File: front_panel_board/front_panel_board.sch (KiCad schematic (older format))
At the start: 4 parts

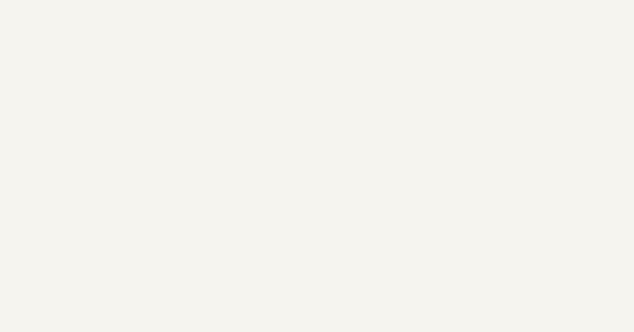
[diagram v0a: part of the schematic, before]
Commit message: update TODO on front panel board (headphone amp)
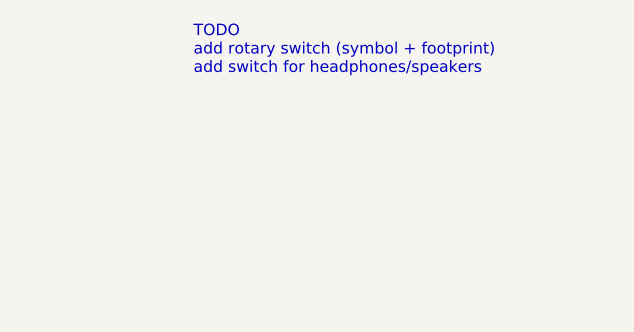
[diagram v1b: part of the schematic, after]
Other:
- note added: "TODO\nadd rotary switch (symbol + footprint)\nadd switch for headphones/speakers"
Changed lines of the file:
@@
 	1    0    0    -1
 $EndComp
+Text Notes 8800 1000 0    50   ~ 0
+TODO\nadd rotary switch (symbol + footprint)\nadd switch for headphones/speakers
 $EndSCHEMATC

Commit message: draw initial schematic for front panel board. Resistor sizing and component selection still todo
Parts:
- removed J?: Conn_02x04_Odd_Even, symbol Connector_Generic:Conn_02x04_Odd_Even
- added J2: Conn_02x05_Odd_Even, symbol Connector_Generic:Conn_02x05_Odd_Even
- added R1, R2: R, symbol Device:R
- added SW1: SW_Rotary4, symbol Switch_gkeeth:SW_Rotary4
- added SW2: SW_SPST, symbol Switch:SW_SPST
- gave numbers to parts that had none: 3
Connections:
- net labels added: GNDRELAY, Vrelay, input1_select, input2_select, input3_select, input4_select, output_mute_select
- wire segments 0 -> 32
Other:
- note added: "TODO\nadd rotary switch footprint\nsize relay resistors"
- note added: "disables main preamp output\n(headphones unaffected)"
- note added: "input selection switch"
- note added: "output mute switch"
- note added: "power LED"
- note added: "power connector"
- note removed: "TODO\nadd rotary switch (symbol + footprint)\nadd switch for headphones/speakers"
- moved on the sheet: D1, J1, R3

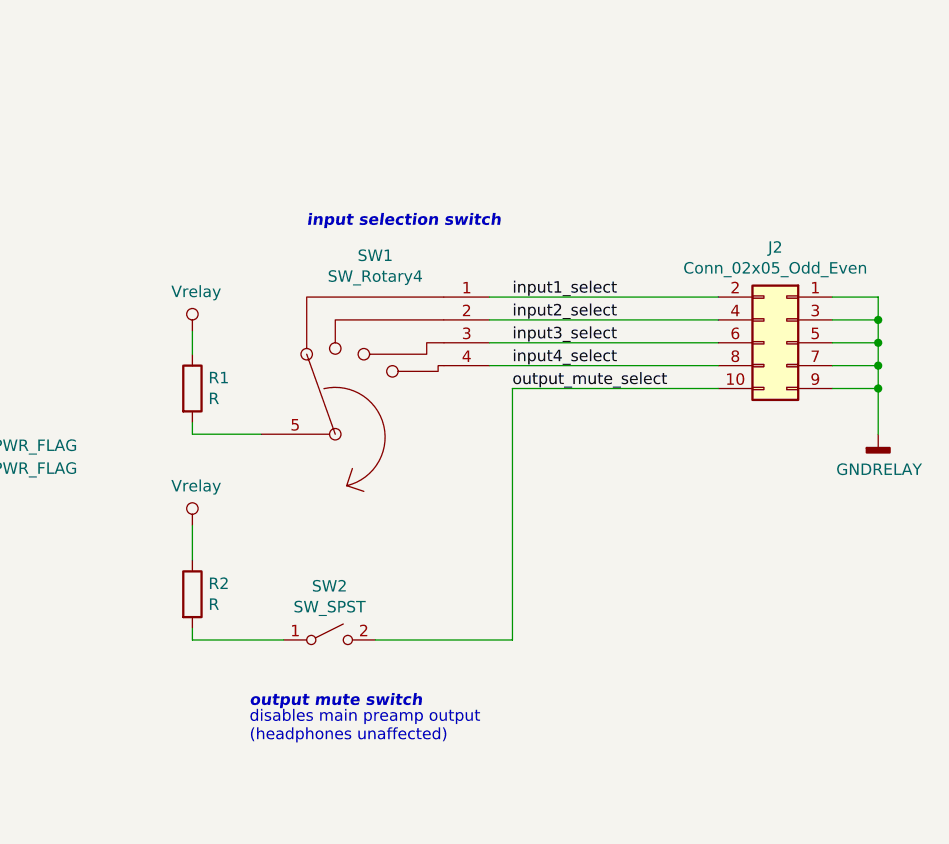
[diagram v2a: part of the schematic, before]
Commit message: change input selection switch to 12-pos with adjustable stops
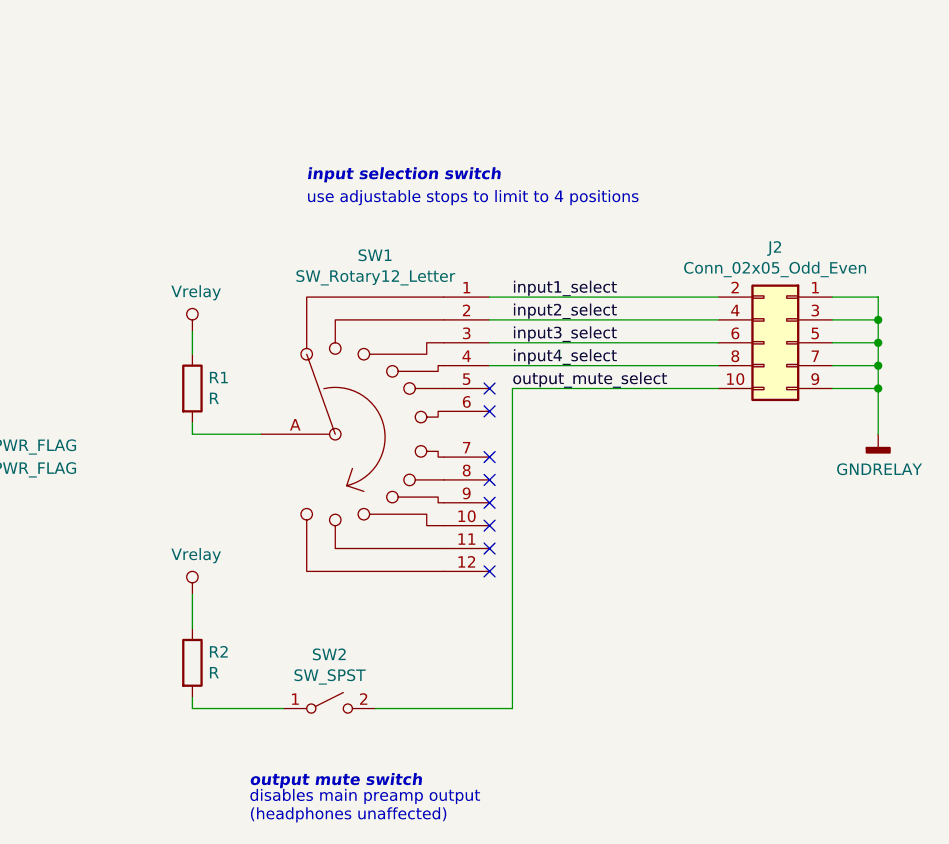
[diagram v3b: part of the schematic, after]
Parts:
- removed SW1: SW_Rotary4, symbol Switch_gkeeth:SW_Rotary4
- added SW1: SW_Rotary12_Letter, symbol Switch_gkeeth:SW_Rotary12_Letter
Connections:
- net input1_select: now also SW1.1
- net input2_select: now also SW1.2
- net input3_select: now also SW1.3
- net input4_select: now also SW1.4
- net at R1.2: now also SW1.A (13)
- no-connect marks 0 -> 8
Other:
- note added: "use adjustable stops to limit to 4 positions"
- moved on the sheet: R2, SW2
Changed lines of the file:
@@
 L Switch:SW_SPST SW2
 U 1 1 5CD2469D
-P 3900 5200
-F 0 "SW2" H 3900 5435 50  0000 C CNN
-F 1 "SW_SPST" H 3900 5344 50  0000 C CNN
-F 2 "" H 3900 5200 50  0001 C CNN
-F 3 "~" H 3900 5200 50  0001 C CNN
-	1    3900 5200
+P 3900 5500
+F 0 "SW2" H 3900 5735 50  0000 C CNN
+F 1 "SW_SPST" H 3900 5644 50  0000 C CNN
+F 2 "" H 3900 5500 50  0001 C CNN
+F 3 "~" H 3900 5500 50  0001 C CNN
+	1    3900 5500
 	1    0    0    -1
 $EndComp
@@
 Wire Wire Line
 	2150 4350 2150 4250
-$Comp
-L Switch_gkeeth:SW_Rotary4 SW1
-U 1 1 5CD232DB
-P 4200 4300
-F 0 "SW1" H 4100 5081 50  0000 C CNN
-F 1 "SW_Rotary4" H 4100 4990 50  0000 C CNN
-F 2 "" H 4000 5000 50  0001 C CNN
-F 3 "http://cdn-reichelt.de/documents/datenblatt/C200/DS-Serie%23LOR.pdf" H 4000 5000 50  0001 C CNN
-	1    4200 4300
-	1    0    0    -1
-$EndComp
 Wire Wire Line
 	4600 3700 5600 3700
@@
 input4_select
 Wire Wire Line
-	4100 5200 4700 5200
-Wire Wire Line
-	4700 5200 4700 4100
+	4100 5500 4700 5500
 Wire Wire Line
 	4700 4100 5600 4100
@@
 L power_gkeeth:Vrelay #PWR0104
 U 1 1 5CD3104E
-P 3300 4700
-F 0 "#PWR0104" H 3300 4550 50  0001 C CNN
-F 1 "Vrelay" H 3317 4873 50  0000 C CNN
-F 2 "" H 3300 4700 50  0001 C CNN
-F 3 "" H 3300 4700 50  0001 C CNN
-	1    3300 4700
+P 3300 5000
+F 0 "#PWR0104" H 3300 4850 50  0001 C CNN
+F 1 "Vrelay" H 3317 5173 50  0000 C CNN
+F 2 "" H 3300 5000 50  0001 C CNN
+F 3 "" H 3300 5000 50  0001 C CNN
+	1    3300 5000
 	1    0    0    -1
 $EndComp
@@
 L Device:R R2
 U 1 1 5CD315AC
-P 3300 5000
-F 0 "R2" H 3370 5046 50  0000 L CNN
-F 1 "R" H 3370 4955 50  0000 L CNN
-F 2 "" V 3230 5000 50  0001 C CNN
-F 3 "~" H 3300 5000 50  0001 C CNN
-	1    3300 5000
-	1    0    0    -1
-$EndComp
-Wire Wire Line
-	3300 5150 3300 5200
-Wire Wire Line
-	3300 5200 3700 5200
-Wire Wire Line
-	3300 4850 3300 4700
-Text Notes 3550 5650 0    50   ~ 0
+P 3300 5300
+F 0 "R2" H 3370 5346 50  0000 L CNN
+F 1 "R" H 3370 5255 50  0000 L CNN
+F 2 "" V 3230 5300 50  0001 C CNN
+F 3 "~" H 3300 5300 50  0001 C CNN
+	1    3300 5300
+	1    0    0    -1
+$EndComp
+Wire Wire Line
+	3300 5450 3300 5500
+Wire Wire Line
+	3300 5500 3700 5500
+Wire Wire Line
+	3300 5150 3300 5000
+Text Notes 3550 6000 0    50   ~ 0
 disables main preamp output\n(headphones unaffected)
-Text Notes 3550 5500 0    50   Italic 10
+Text Notes 3550 5850 0    50   Italic 10
 output mute switch
-Text Notes 3800 3400 0    50   Italic 10
+Text Notes 3800 3200 0    50   Italic 10
 input selection switch
 $Comp
@@
 	2150 4350 2300 4350
 Connection ~ 2150 4350
+$Comp
+L Switch_gkeeth:SW_Rotary12_Letter SW1
+U 1 1 5CD4AABC
+P 4200 4300
+F 0 "SW1" H 4100 5081 50  0000 C CNN
+F 1 "SW_Rotary12_Letter" H 4100 4990 50  0000 C CNN
+F 2 "" H 4000 5000 50  0001 C CNN
+F 3 "http://cdn-reichelt.de/documents/datenblatt/C200/DS-Serie%23LOR.pdf" H 4000 5000 50  0001 C CNN
+	1    4200 4300
+	1    0    0    -1
+$EndComp
+NoConn ~ 4600 4100
+NoConn ~ 4600 4200
+NoConn ~ 4600 4400
+NoConn ~ 4600 4500
+NoConn ~ 4600 4600
+NoConn ~ 4600 4700
+NoConn ~ 4600 4800
+NoConn ~ 4600 4900
+Wire Wire Line
+	4700 4100 4700 5500
+Text Notes 3800 3300 0    50   ~ 0
+use adjustable stops to limit to 4 positions
 $EndSCHEMATC

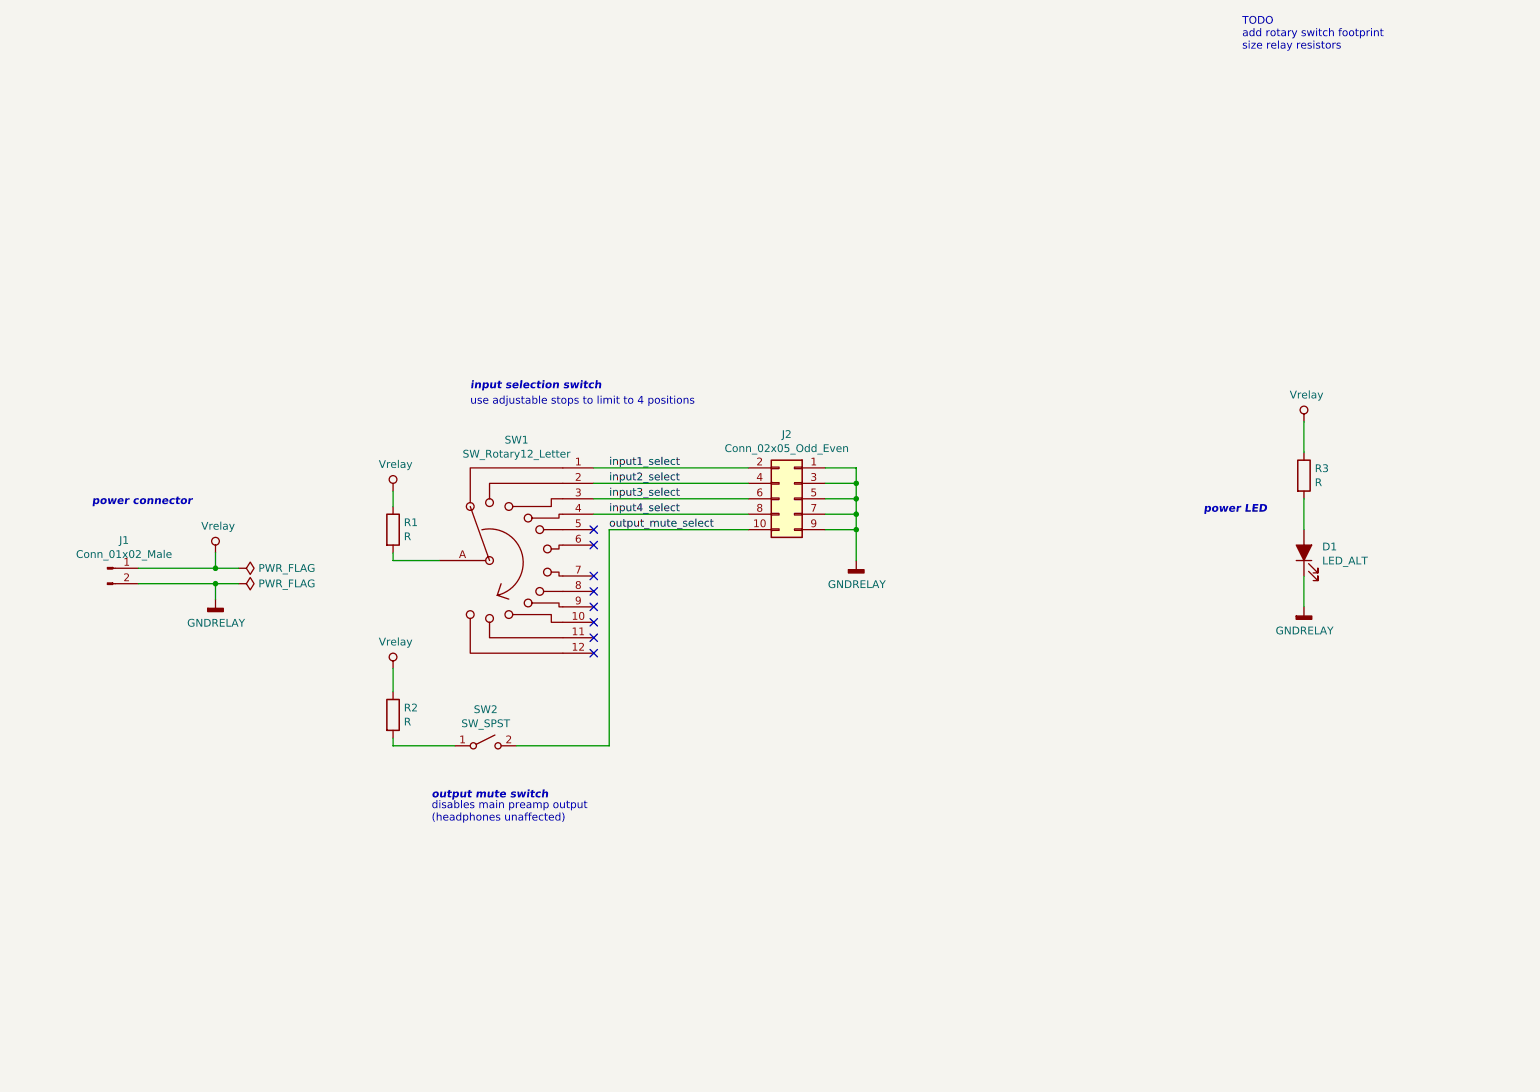
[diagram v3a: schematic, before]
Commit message: complete schematic except footprint for output mute switch
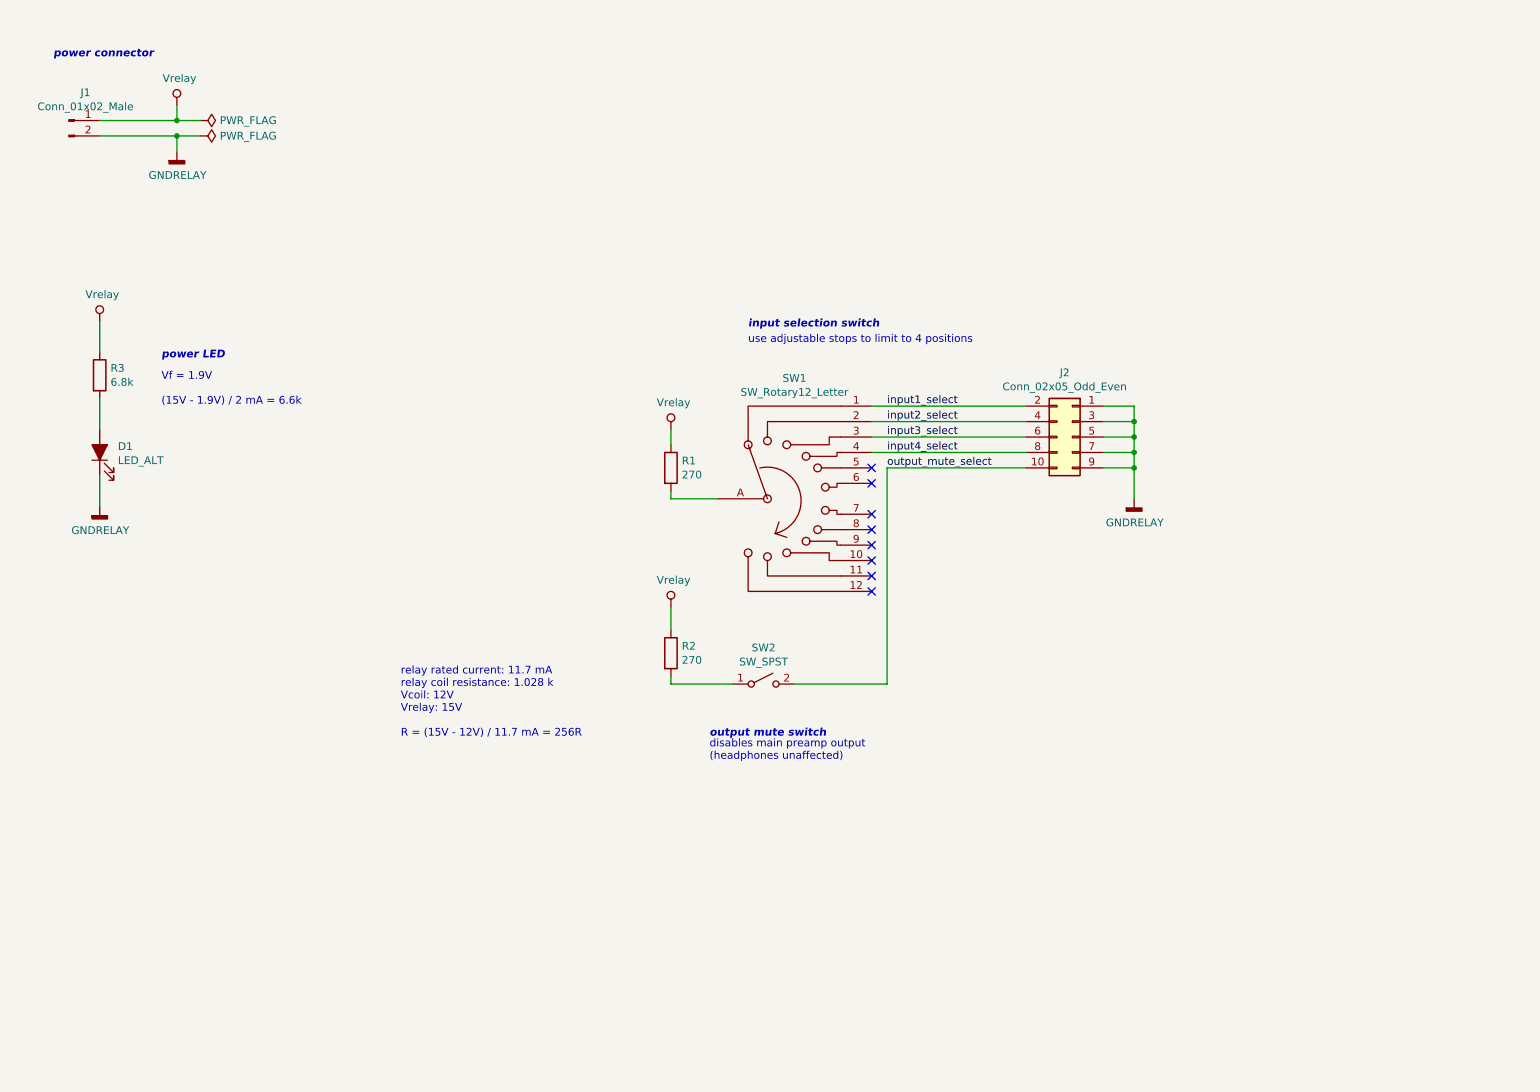
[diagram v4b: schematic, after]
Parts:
- D1: footprint (none) -> LED_THT:LED_D5.0mm; Distributor (none) -> Digikey; Distributor PN (none) -> 754-1265-ND; Manufacturer (none) -> Kingbright; Manufacturer PN (none) -> WP7113LGD; URL (none) -> https://www.digikey.com/product-detail/en/kingbright/WP7113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; Unit Price (none) -> 0.48
- J1: footprint (none) -> Connector_Molex_SL:Molex_SL_A-70543-0001_1x02_P2.54mm_Vertical
- J2: footprint (none) -> Connector_Molex_C-Grid:Molex_C-Grid_70246-1001_2x05_P2.54mm_Vertical
- R1, R2: value R -> 270; footprint (none) -> Resistor_SMD:R_0603_1608Metric_Pad1.05x0.95mm_HandSolder; Distributor (none) -> Digikey; Distributor PN (none) -> 311-2504-1-ND; Manufacturer (none) -> Yageo; Manufacturer PN (none) -> RT0603DRE07270RL; URL (none) -> https://www.digikey.com/product-detail/en/yageo/RT0603DRE07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; Unit Price (none) -> 0.12
- R3: value R -> 6.8k; footprint (none) -> Resistor_SMD:R_0603_1608Metric_Pad1.05x0.95mm_HandSolder; Distributor (none) -> Digikey; Distributor PN (none) -> YAG5968CT-ND; Manufacturer (none) -> Yageo; Manufacturer PN (none) -> YAG5968CT-ND; URL (none) -> https://www.digikey.com/product-detail/en/yageo/RT0603FRE07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; Unit Price (none) -> 0.10
- SW1: footprint (none) -> Button_Switch_THT_gkeeth:SW_Rotary12_C&K_A112xxxxCxx
- SW2: Distributor (none) -> Digikey; Distributor PN (none) -> 360-3243-ND; Manufacturer (none) -> NKK; Manufacturer PN (none) -> M2011SS1W03; URL (none) -> https://www.digikey.com/product-detail/en/nkk-switches/M201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; Unit Price (none) -> 4.64
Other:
- note added: "Vf = 1.9V\n\n(15V - 1.9V) / 2 mA = 6.6k"
- note added: "relay rated current: 11.7 mA\nrelay coil resistance: 1.028 k\nVcoil: 12V\nVrelay: 15V\n\nR = (15V - 12V) / 11.7 mA = 256R"
- note removed: "TODO\nadd rotary switch footprint\nsize relay resistors"
- moved on the sheet: D1, J1, J2, R1, R3, SW1, SW2

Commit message: add footprint for toggle switch and do inital layout (exact switch/LED placement tbd)
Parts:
- SW2: footprint (none) -> Button_Switch_THT_gkeeth:SW_Toggle_SPST_NKK_M2011xxx03
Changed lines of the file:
@@
 F 0 "SW2" H 5700 5335 50  0000 C CNN
 F 1 "SW_SPST" H 5700 5244 50  0000 C CNN
-F 2 "" H 5700 5100 50  0001 C CNN
+F 2 "Button_Switch_THT_gkeeth:SW_Toggle_SPST_NKK_M2011xxx03" H 5700 5100 50  0001 C CNN
 F 3 "http://www.nkkswitches.com/pdf/MtogglesBushing.pdf" H 5700 5100 50  0001 C CNN
 F 4 "NKK" H 5700 5100 50  0001 C CNN "Manufacturer"

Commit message: hide fab layer contents for creative commons symbols
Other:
- note added: "TODO\nChange switch to 8pos, 45deg model? A12505RNCQ\nadd connector to optionally bypass toggle switch?"
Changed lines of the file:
@@
 Text Notes 1800 3300 0    50   ~ 0
 Vf = 1.9V\n\n(15V - 1.9V) / 2 mA = 6.6k
+Text Notes 8000 1100 0    50   ~ 0
+TODO\nChange switch to 8pos, 45deg model? A12505RNCQ\nadd connector to optionally bypass toggle switch?
 $EndSCHEMATC

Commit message: add license info to schematics & layouts, including made with kicad logo, as well as project info to silkscreen
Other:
- note added: "CC-BY-SA 4.0"
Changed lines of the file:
@@
 Text Notes 8000 1100 0    50   ~ 0
 TODO\nChange switch to 8pos, 45deg model? A12505RNCQ\nadd connector to optionally bypass toggle switch?
+$Comp
+L Graphic:Logo_Open_Hardware_Large #LOGO?
+U 1 1 5D0E05C4
+P 5500 7150
+F 0 "#LOGO?" H 5500 7650 50  0001 C CNN
+F 1 "Logo_Open_Hardware_Large" H 5500 6750 50  0001 C CNN
+F 2 "" H 5500 7150 50  0001 C CNN
+F 3 "~" H 5500 7150 50  0001 C CNN
+	1    5500 7150
+	1    0    0    -1
+$EndComp
+Text Notes 5250 7650 0    50   ~ 0
+CC-BY-SA 4.0
 $EndSCHEMATC
